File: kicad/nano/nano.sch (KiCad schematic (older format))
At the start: 47 parts, among them J1 I2C, J2 PROGPADS, U1 AP6502A, U2 PIC16F1459, U3 AVALON, U4 MCP1700, U5 AP7217D/RT9166A, U6 74AUP1G02, X1 ASDMB

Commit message: update nano design files, add fix1
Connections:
- net at D1.2 (K), U1.1 (BST): now also C3.1; no longer C3.2, L1.1
- net at U1.3 (SW): now also C3.2, L1.1; no longer C3.1
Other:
- moved on the sheet: C3, D1
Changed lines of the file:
@@
-EESchema Schematic File Version 2  date Wed 22 May 2013 09:08:58 AM ICT
+EESchema Schematic File Version 2  date Thu 20 Jun 2013 08:43:58 AM ICT
 LIBS:k16
 LIBS:nano
@@
 Sheet 1 1
 Title "asic-v1.sch"
-Date "22 may 2013"
+Date "20 jun 2013"
 Rev ""
 Comp ""
@@
 	1    8173 4173
 	1    0    0    -1
-$EndComp
-$Comp
-L C-EU C3
-U 1 1 517F6EA0
-P 4553 4043
-F 0 "C3" V 4533 3942 22  0000 L BNN
-F 1 "6.8nF" V 4559 3876 22  0000 L CNN
-F 2 "" H 4553 4043 60  0001 C CNN
-F 3 "" H 4553 4043 60  0001 C CNN
-	1    4553 4043
-	0    -1   -1   0
 $EndComp
 $Comp
@@
 U 1 1 517F6E0C
 P 4191 4083
-F 0 "U1" H 4287 4275 27  0000 L BNN
-F 1 "AP6502A" H 4287 4339 27  0000 L BNN
+F 0 "U1" H 4179 4277 27  0000 L BNN
+F 1 "AP6502A" H 4184 4323 27  0000 L BNN
 F 2 "" H 4191 4083 60  0001 C CNN
 F 3 "" H 4191 4083 60  0001 C CNN
@@
 Wire Wire Line
 	8333 4703 8333 4893
-Wire Wire Line
-	4617 3918 4617 4043
-Wire Wire Line
-	4479 3987 4712 3987
-Connection ~ 4617 3987
 Wire Wire Line
 	5837 4047 5901 4047
@@
 Connection ~ 4832 4103
 Wire Wire Line
-	4521 4043 4481 4043
-Wire Wire Line
 	4481 4168 4519 4168
 Wire Wire Line
@@
 VCC
 Wire Wire Line
-	4617 3778 4617 3716
-Text Label 4617 3716 0    22   ~ 0
+	4537 3783 4537 3721
+Text Label 4537 3721 0    22   ~ 0
 VIN
 $Comp
@@
 L SL02-DIODE D1
 U 1 1 5188B154
-P 4617 3883
-F 0 "D1" V 4528 3965 40  0000 C CNN
-F 1 "SL02" V 4586 4001 40  0000 C CNN
-F 2 "~" H 4617 3883 60  0000 C CNN
-F 3 "~" H 4617 3883 60  0000 C CNN
-	1    4617 3883
+P 4537 3888
+F 0 "D1" V 4448 3970 22  0000 C CNN
+F 1 "SL02" V 4478 3988 22  0000 C CNN
+F 2 "~" H 4537 3888 60  0000 C CNN
+F 3 "~" H 4537 3888 60  0000 C CNN
+	1    4537 3888
 	0    1    1    0
 $EndComp
@@
 Text Label 7015 3911 0    20   ~ 0
 VCC
+Wire Wire Line
+	4670 4043 4481 4043
+Wire Wire Line
+	4479 3987 4537 3987
+Wire Wire Line
+	4633 3987 4712 3987
+$Comp
+L C-EU C3
+U 1 1 517F6EA0
+P 4569 3987
+F 0 "C3" V 4619 3914 22  0000 L BNN
+F 1 "6.8nF" V 4638 3881 22  0000 L CNN
+F 2 "" H 4569 3987 60  0001 C CNN
+F 3 "" H 4569 3987 60  0001 C CNN
+	1    4569 3987
+	0    -1   -1   0
+$EndComp
+Connection ~ 4670 3987
+Wire Wire Line
+	4670 3987 4670 4043
+Wire Wire Line
+	4537 3987 4537 3923
 $EndSCHEMATC

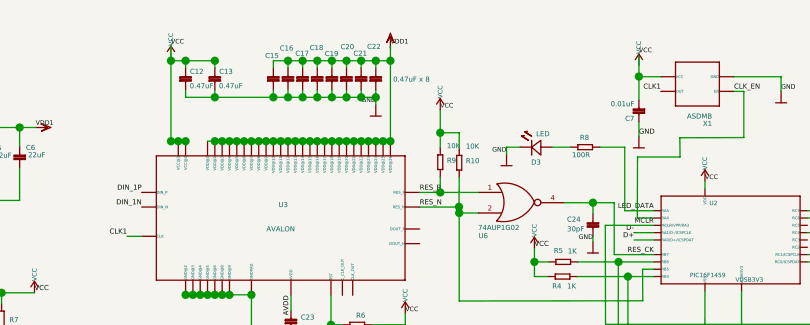
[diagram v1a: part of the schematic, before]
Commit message: update K16 brd for PIC VCC fix, 0.2.1
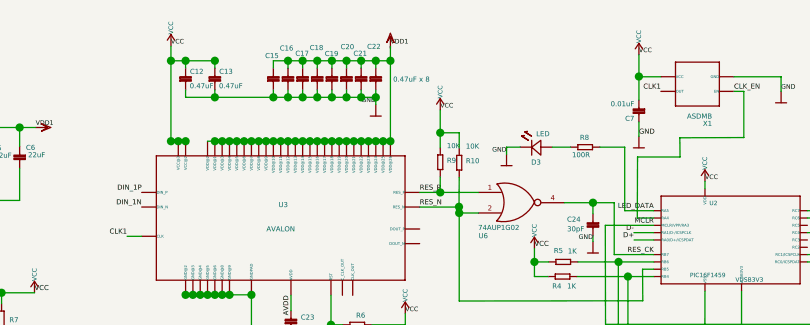
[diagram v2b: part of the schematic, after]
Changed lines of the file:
@@
-EESchema Schematic File Version 2  date Thu 20 Jun 2013 08:43:58 AM ICT
+EESchema Schematic File Version 2  date Fri 21 Jun 2013 07:25:55 AM ICT
 LIBS:k16
 LIBS:nano
@@
 encoding utf-8
 Sheet 1 1
-Title "asic-v1.sch"
-Date "20 jun 2013"
+Title "Klondike 1 ASIC Miner"
+Date "21 jun 2013"
 Rev ""
 Comp ""
@@
 L VCC #VCC08
 U 1 1 517F6E1C
-P 5837 3631
-F 0 "#VCC08" V 5805 3600 22  0001 L BNN
-F 1 "VCC" H 5837 3631 60  0001 C CNN
-F 2 "" H 5837 3631 60  0001 C CNN
-F 3 "" H 5837 3631 60  0001 C CNN
-	1    5837 3631
+P 5837 3581
+F 0 "#VCC08" V 5805 3550 22  0001 L BNN
+F 1 "VCC" H 5837 3581 60  0001 C CNN
+F 2 "" H 5837 3581 60  0001 C CNN
+F 3 "" H 5837 3581 60  0001 C CNN
+	1    5837 3581
 	1    0    0    -1
 $EndComp
@@
 L VCC #VCC09
 U 1 1 517F6E3C
-P 7884 3666
-F 0 "#VCC09" V 7852 3635 22  0001 L BNN
-F 1 "VCC" H 7884 3666 60  0001 C CNN
-F 2 "" H 7884 3666 60  0001 C CNN
-F 3 "" H 7884 3666 60  0001 C CNN
-	1    7884 3666
-	1    0    0    -1
-$EndComp
+P 7884 3619
+F 0 "#VCC09" V 7852 3588 22  0001 L BNN
+F 1 "VCC" H 7884 3619 60  0001 C CNN
+F 2 "" H 7884 3619 60  0001 C CNN
+F 3 "" H 7884 3619 60  0001 C CNN
+	1    7884 3619
+	1    0    0    -1
+$EndComp

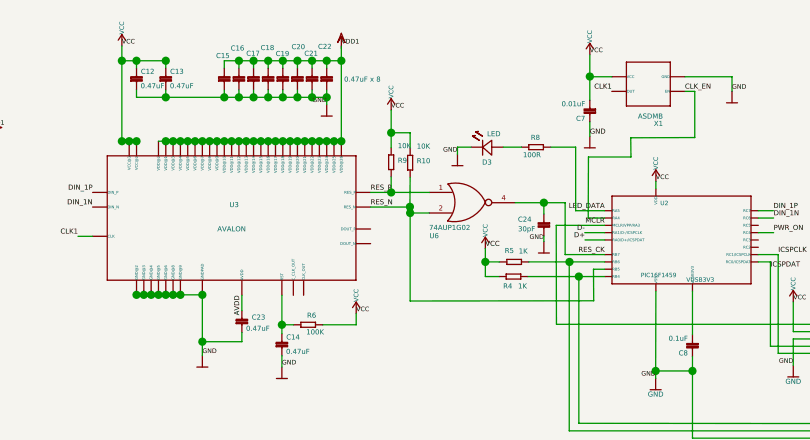
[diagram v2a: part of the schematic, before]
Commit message: update resistors, parts list, v0.2.2
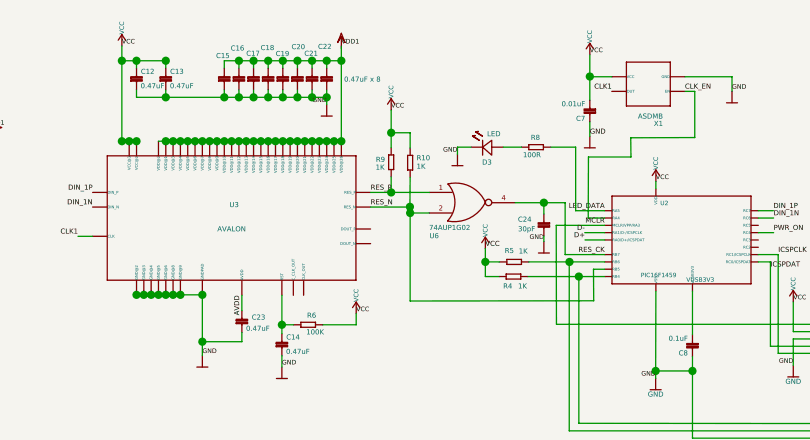
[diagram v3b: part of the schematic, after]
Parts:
- R10, R9: value 10K -> 1K
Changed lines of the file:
@@
-EESchema Schematic File Version 2  date Fri 21 Jun 2013 07:25:55 AM ICT
+EESchema Schematic File Version 2  date Tue 25 Jun 2013 12:06:05 AM ICT
 LIBS:k16
 LIBS:nano
@@
 Sheet 1 1
 Title "Klondike 1 ASIC Miner"
-Date "21 jun 2013"
+Date "24 jun 2013"
 Rev ""
 Comp ""
@@
 U 1 1 519C27F1
 P 7098 4141
-F 0 "R10" V 7103 4170 22  0000 L BNN
-F 1 "10K" V 7039 4170 22  0000 L BNN
+F 0 "R10" V 7090 4169 22  0000 L BNN
+F 1 "1K" V 7127 4169 22  0000 L BNN
 F 2 "" H 7098 4141 60  0001 C CNN
 F 3 "" H 7098 4141 60  0001 C CNN
@@
 U 1 1 519C27F7
 P 7015 4139
-F 0 "R9" V 7020 4168 22  0000 L BNN
-F 1 "10K" V 6956 4168 22  0000 L BNN
+F 0 "R9" V 7016 4072 22  0000 L BNN
+F 1 "1K" V 7050 4071 22  0000 L BNN
 F 2 "" H 7015 4139 60  0001 C CNN
 F 3 "" H 7015 4139 60  0001 C CNN

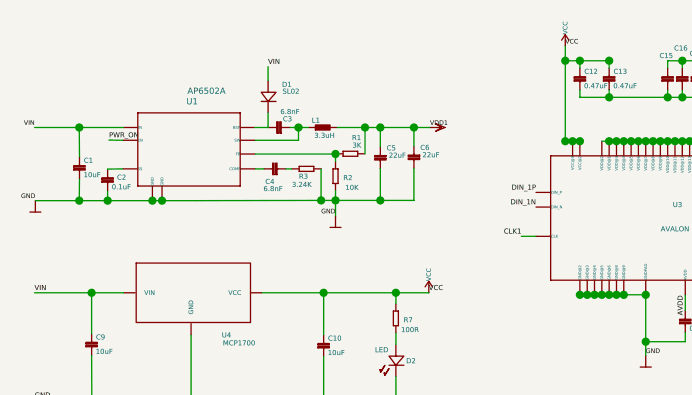
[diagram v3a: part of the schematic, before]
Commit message: fixes for 300 MHz, fix K1 parts list
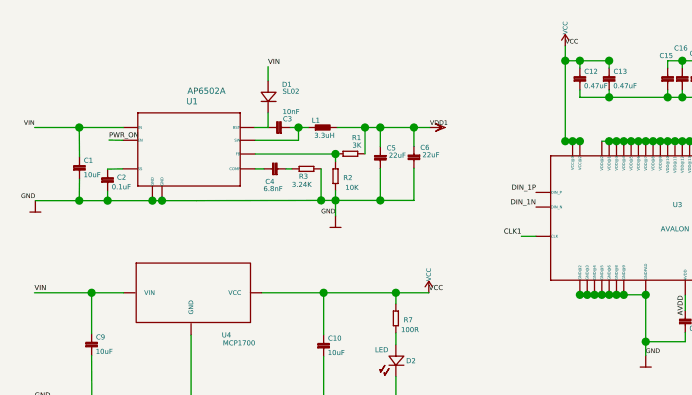
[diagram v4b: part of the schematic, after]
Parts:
- C3: value 6.8nF -> 10nF
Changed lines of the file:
@@
-EESchema Schematic File Version 2  date Tue 25 Jun 2013 12:06:05 AM ICT
+EESchema Schematic File Version 2  date Sun 07 Jul 2013 03:35:31 AM ICT
 LIBS:k16
 LIBS:nano
@@
 Sheet 1 1
 Title "Klondike 1 ASIC Miner"
-Date "24 jun 2013"
+Date "6 jul 2013"
 Rev ""
 Comp ""
@@
 P 4569 3987
 F 0 "C3" V 4619 3914 22  0000 L BNN
-F 1 "6.8nF" V 4638 3881 22  0000 L CNN
+F 1 "10nF" V 4638 3881 22  0000 L CNN
 F 2 "" H 4569 3987 60  0001 C CNN
 F 3 "" H 4569 3987 60  0001 C CNN

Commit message: update K1 parts, schematic
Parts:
- removed J1: I2C, pinhead-1X03, symbol PINHD-1X3
- removed J2: PROGPADS, ~, symbol PROGPADS
- removed U6: 74AUP1G02, ~, symbol 74AUP1G02
- added C25: 0.01uF, symbol C-EU
- added C26: 0.1uF, symbol C-EU
- added J1: PINHD-1X4, pinhead-1X04, symbol PINHD-1X4
- added J2: ~, symbol MINIUSB
- added L2: 60R / 100 MHz, symbol R-EU
- added L3: 120R @ 100 MHz, symbol R-EU
- added L4: 120R / 100 MHz, symbol R-EU
- added L5, L6: 220R @ 100 MHz, symbol R-EU
- added PRG1: ~, symbol PROGPADS
- added R11: 100R, symbol R-EU
- added R12: 1K, symbol R-EU
- added RT1: 2.2K, symbol R-EU
- added U6: 74AUP2G02, ~, symbol 74AUP2G02
- added U7: NL27WZ14, symbol NL27WZ14
- C22: value 0.47uF x 8 -> 0.47uF
- U2: value PIC16F1459 -> PIC16LF1459
- X1: value ASDMB -> ASMDB
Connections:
- net AVDD: now also L2.2; no longer C23.1, U3.P$42 (AVDD)
- net D+: now also J2.3 (D+), L4.2; no longer U2.19 (RA0/D+/ICSPDAT)
- net D-: now also J2.2 (D-), L3.2; no longer U2.18 (RA1/D-/ICSPCLK)
- net GND: now also C7.2, R7.1, R8.2, C25.2, C26.1, J1.1, L5.1, PRG1.3 (GND), R12.2, U6.4 (GND), U6.4 (GND), U7.2 (GND), U7.2 (GND); no longer C7.1, D2.2 (K), D3.2 (K)
- net ICSPCLK: now also PRG1.5 (ICSPCLK)
- net ICSPDAT: now also PRG1.4 (ICSPDAT)
- net LED_DATA: now also D3.1 (A); no longer R8.1
- net MCLR: now also PRG1.1 (MCLR)
- net PWR_ON: now also U2.5 (RC5); no longer U2.6 (RC4)
- net RES_CK: now also U7.4; no longer C24.2
- net RES_N: now also U6.2 (B), U7.1; no longer U2.12 (RB5)
- net RES_P: now also U6.1 (A)
- net VCC: now also C7.1, R4.1, R5.1, C25.1, C26.2, PRG1.2 (VCC), RT1.1, U6.8 (VCC), U6.8 (VCC), U7.5 (VCC), U7.5 (VCC); no longer C7.2, R4.2, R5.2, R7.2
- net VIN: now also L6.1
- net THERM: now reaches U2.14 (RC2)
- net THERM: now also R12.1, RT1.2
- net LED_PWR: now reaches D2.1 (A)
- net LED_PWR: now also U2.6 (RC4); no longer R7.1
- net SCL: no longer names the net of U2.11 (RB6)
- net SCL: now also R5.2, J1.3; no longer R5.1
- net SDA: no longer names the net of U2.13 (RB4)
- net SDA: now also R4.2, J1.4; no longer R4.1
- new net: C23.1, L2.1, U3.P$42 (AVDD)
- new net: D2.2 (K), R7.2
- new net: J2.1 (5V), L6.2
- new net: J2.5 (GND), J2.S1 (GND), J2.S2 (GND), J2.S3 (GND), J2.S4 (GND), L5.2
- new net: L3.1, U2.18 (RA1/D-/ICSPCLK)
- new net: L4.1, U2.19 (RA0/D+/ICSPDAT)
- new net: D3.2 (K), R8.1
- new net: C24.2, R11.1, U6.5 (A)
- new net: U6.3 (Y), U7.3
- new net RES_DI: U2.12 (RB5), U7.6
- new net RES_PN: R11.2, U6.6 (B), U6.7 (Y)
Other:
- note added: "I2C BUS"
- note added: "ICSP (pads)"
- note added: "USB"
- moved on the sheet: C1, C10, C11, C12, C13, C14, C15, C16, C17, C18, C19, C2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

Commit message: update K1 to 0.3.0
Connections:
- net SCK: now reaches R5.2, U2.11 (RB6)
- net SCK: now also J1.2; no longer J1.3
- net SDA: now reaches R4.2, U2.13 (RB4)
- net SDA: now also J1.3; no longer J1.4
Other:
- moved on the sheet: J1
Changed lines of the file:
@@
-EESchema Schematic File Version 2  date Thu 18 Jul 2013 12:04:05 AM ICT
+EESchema Schematic File Version 2  date Tue 23 Jul 2013 06:09:05 PM ICT
 LIBS:k16
 LIBS:nano
@@
 Sheet 1 1
 Title "Klondike 1 ASIC Miner"
-Date "17 jul 2013"
+Date "23 jul 2013"
 Rev ""
 Comp ""
@@
 Wire Wire Line
 	2937 2937 2937 2873
-Text Notes 10174 4343 0    22   ~ 0
+Text Notes 10186 4329 0    22   ~ 0
 I2C BUS
 Text Notes 10246 5085 0    22   ~ 0
@@
 L PINHD-1X4 J1
 U 1 1 51E594E1
-P 10128 4298
-F 0 "J1" H 10048 4370 22  0000 L BNN
-F 1 "PINHD-1X4" H 10143 4153 50  0001 L BNN
-F 2 "pinhead-1X04" H 10128 4448 50  0001 C CNN
-F 3 "~" H 10128 4298 60  0000 C CNN
-	1    10128 4298
+P 10128 4330
+F 0 "J1" H 10048 4402 22  0000 L BNN
+F 1 "PINHD-1X4" H 10143 4185 50  0001 L BNN
+F 2 "pinhead-1X04" H 10128 4480 50  0001 C CNN
+F 3 "~" H 10128 4330 60  0000 C CNN
+	1    10128 4330
 	1    0    0    -1
 $EndComp
@@
 	9535 3821 9215 3821
 Wire Wire Line
-	9896 4266 9896 4720
+	9896 4606 9895 4297
+Wire Wire Line
+	9896 4606 9896 4720
 Connection ~ 9896 4606
 Wire Wire Line
 	8347 4045 8348 4364
 Wire Wire Line
-	8348 4364 10098 4363
+	8348 4364 10096 4362
 Connection ~ 8347 4045
-Connection ~ 9599 4269
 Wire Wire Line
 	9471 4752 10079 4752
@@
 Wire Wire Line
 	8543 4013 8052 4013
-Wire Wire Line
-	9896 4266 10096 4266
-Connection ~ 10096 4266
 Wire Wire Line
 	8150 4422 8150 4489
@@
 Wire Wire Line
 	9817 5003 10015 5003
+Text Label 10096 4362 0    22   ~ 0
+SDA
+Text Label 10096 4330 0    22   ~ 0
+SCK
+Wire Wire Line
+	9895 4297 10096 4298
 $EndSCHEMATC
